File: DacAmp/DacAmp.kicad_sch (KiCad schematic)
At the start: 0 parts

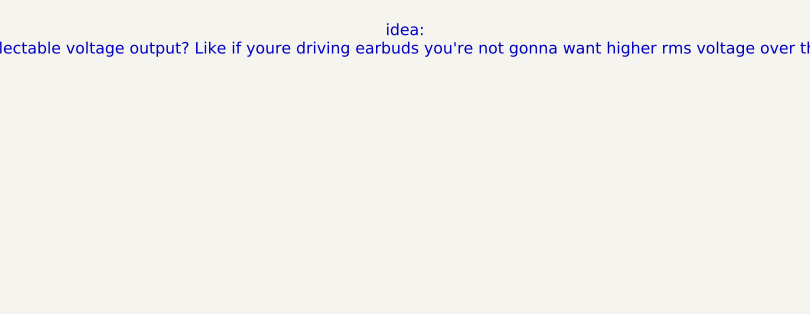
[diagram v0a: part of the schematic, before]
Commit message: add usb + codec
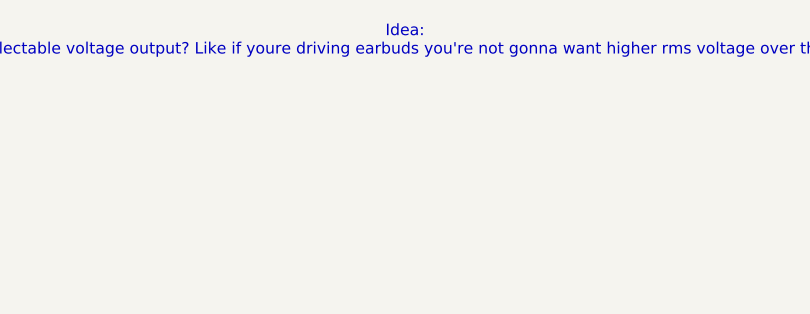
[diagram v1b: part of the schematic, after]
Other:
- note added: "Idea: Make selectable voltage output? Like if youre driving earbuds you're not gonna want higher rms voltage over the thing."
- note removed: "idea: Make selectable voltage output? Like if youre driving earbuds you're not gonna want higher rms voltage over the thing."
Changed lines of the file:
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@@
 	(generator_version "8.0")
 	(paper "A4")
-	(text "idea: \nMake selectable voltage output? Like if youre driving earbuds you're not gonna want higher rms voltage over the thing."
+	(text "Idea: \nMake selectable voltage output? Like if youre driving earbuds you're not gonna want higher rms voltage over the thing."
 		(exclude_from_sim no)
 		(at 217.424 24.13 0)

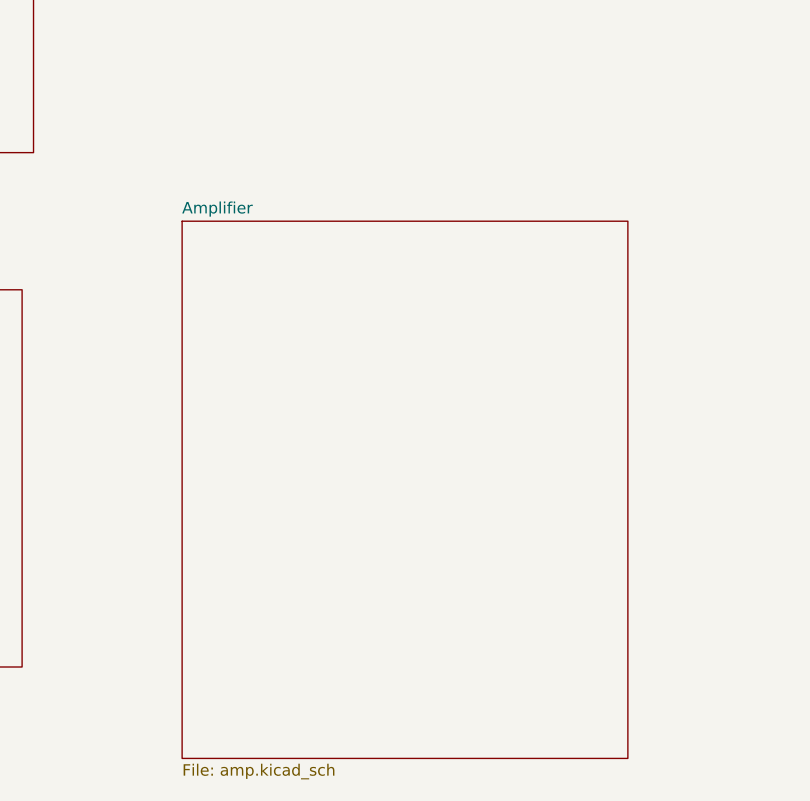
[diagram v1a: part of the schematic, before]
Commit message: add basic analog parts
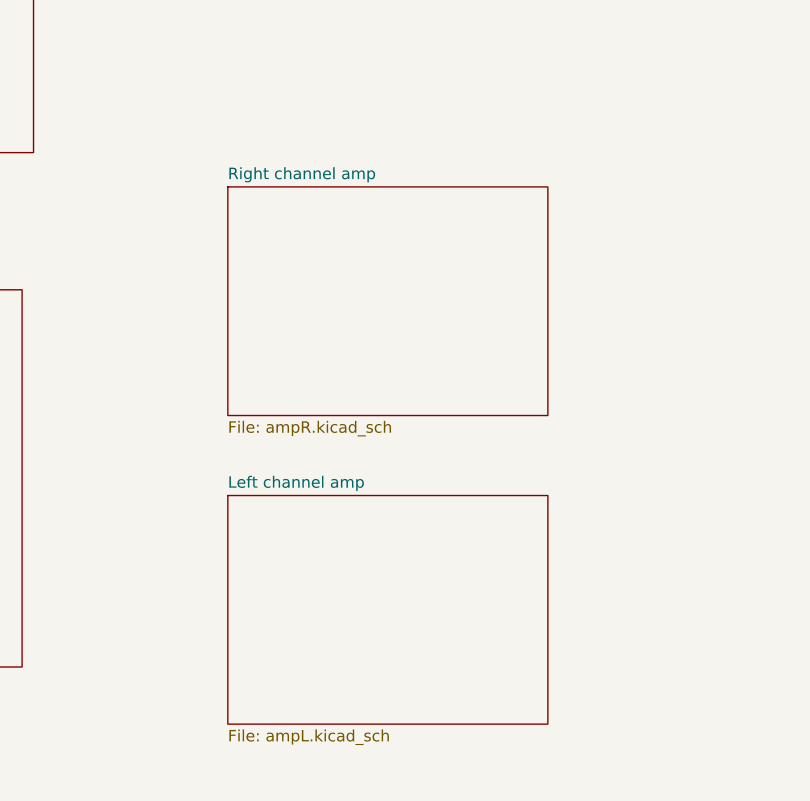
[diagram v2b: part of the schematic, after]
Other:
- removed sheet Amplifier
- added sheet Left channel amp (ampL.kicad_sch)
- added sheet Right channel amp (ampR.kicad_sch)
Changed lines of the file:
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@@
-	)
-	(sheet
-		(at 172.72 74.93)
-		(size 49.53 59.69)
-		(fields_autoplaced yes)
-		(stroke
-			(width 0.1524)
-			(type solid)
-		)
-		(fill
-			(color 0 0 0 0.0000)
-		)
-		(property "Sheetname" "Amplifier"
-			(at 172.72 74.2184 0)
-			(effects
-				(font
-					(size 1.27 1.27)
-				)
-				(justify left bottom)
-			)
-		)
-		(property "Sheetfile" "amp.kicad_sch"
-			(at 172.72 135.2046 0)
-			(effects
-				(font
-					(size 1.27 1.27)
-				)
-				(justify left top)
-			)
-		)
-		(instances
-			(project "DacAmp"
-				(path "/d6da33f4-6bef-4098-a08b-0ea38da216b8"
-					(page "4")
-				)
-			)
-		)
 	)
 	(sheet
@@
 				(path "/d6da33f4-6bef-4098-a08b-0ea38da216b8"
 					(page "2")
+				)
+			)
+		)
+	)
+	(sheet
+		(at 177.8 71.12)
+		(size 35.56 25.4)
+		(fields_autoplaced yes)
+		(stroke
+			(width 0.1524)
+			(type solid)
+		)
+		(fill
+			(color 0 0 0 0.0000)
+		)
+		(property "Sheetname" "Right channel amp"
+			(at 177.8 70.4084 0)
+			(effects
+				(font
+					(size 1.27 1.27)
+				)
+				(justify left bottom)
+			)
+		)
+		(property "Sheetfile" "ampR.kicad_sch"
+			(at 177.8 97.1046 0)
+			(effects
+				(font
+					(size 1.27 1.27)
+				)
+				(justify left top)
+			)
+		)
+		(instances
+			(project "DacAmp"
+				(path "/d6da33f4-6bef-4098-a08b-0ea38da216b8"
+					(page "5")
 				)
 			)
@@
 				)
 			)
+		)
+	)
+	(sheet
+		(at 177.8 105.41)
+		(size 35.56 25.4)
+		(fields_autoplaced yes)
+		(stroke
+			(width 0.1524)
+			(type solid)
+		)
+		(fill
+			(color 0 0 0 0.0000)
+		)
+		(property "Sheetname" "Left channel amp"
+			(at 177.8 104.6984 0)
+			(effects
+				(font
+					(size 1.27 1.27)
+				)
+				(justify left bottom)
+			)
+		)
+		(property "Sheetfile" "ampL.kicad_sch"
+			(at 177.8 131.3946 0)
+			(effects
+				(font
+					(size 1.27 1.27)
+				)
+				(justify left top)
+			)
+		)
+		(instances
+			(project "DacAmp"
+				(path "/d6da33f4-6bef-4098-a08b-0ea38da216b8"
+					(page "6")
+				)
+			)

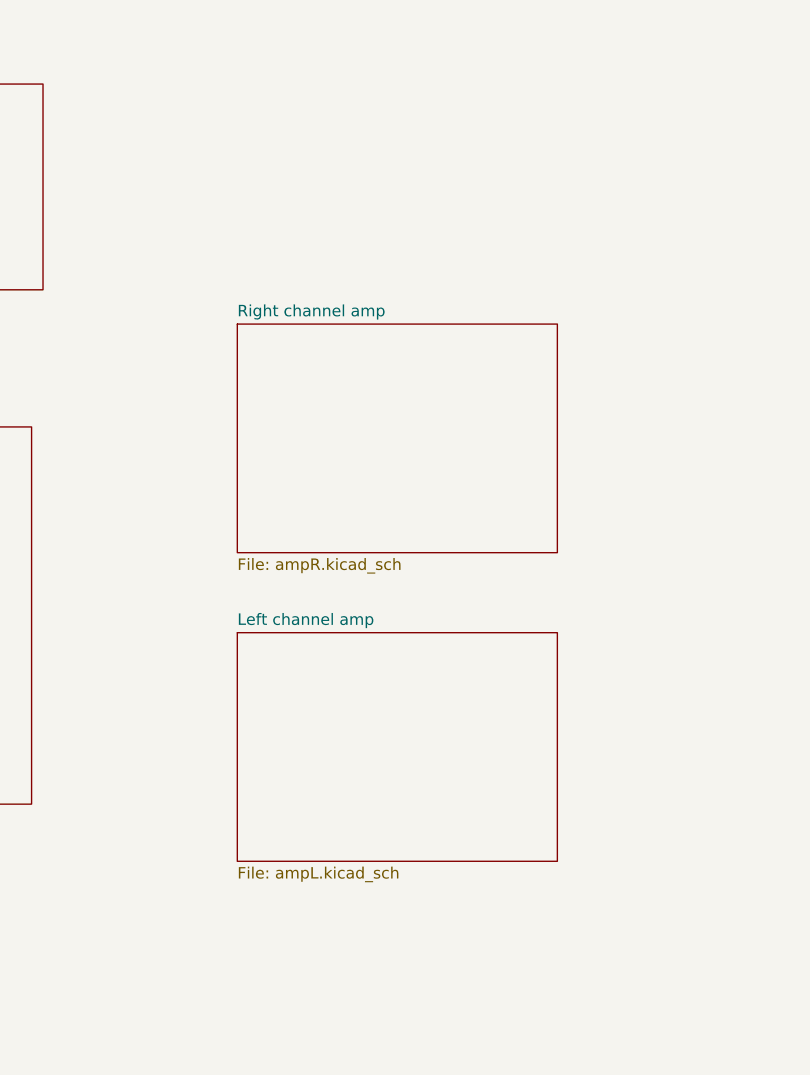
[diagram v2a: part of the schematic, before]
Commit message: add op amps to ampR
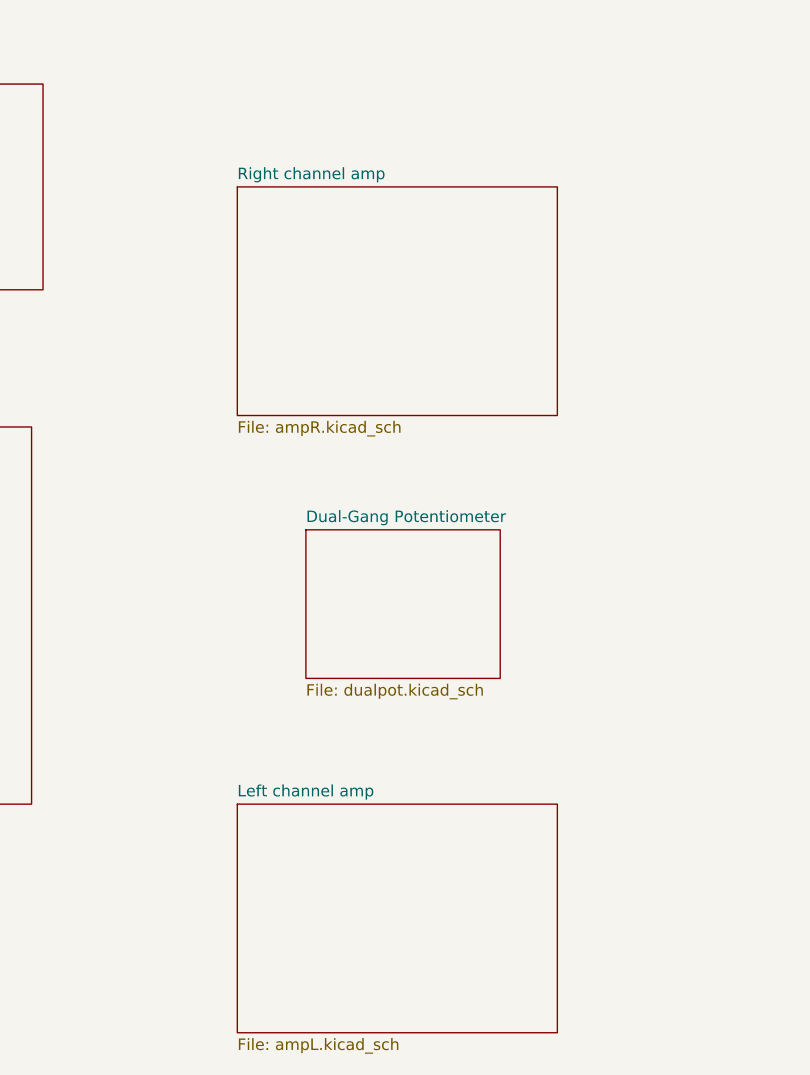
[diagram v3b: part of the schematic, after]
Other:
- added sheet Dual-Gang Potentiometer (dualpot.kicad_sch)
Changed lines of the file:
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@@
 	)
 	(sheet
-		(at 177.8 71.12)
+		(at 177.8 55.88)
 		(size 35.56 25.4)
 		(fields_autoplaced yes)
@@
 		)
 		(property "Sheetname" "Right channel amp"
-			(at 177.8 70.4084 0)
+			(at 177.8 55.1684 0)
 			(effects
 				(font
@@
 		)
 		(property "Sheetfile" "ampR.kicad_sch"
-			(at 177.8 97.1046 0)
+			(at 177.8 81.8646 0)
 			(effects
 				(font
@@
 				(path "/d6da33f4-6bef-4098-a08b-0ea38da216b8"
 					(page "5")
+				)
+			)
+		)
+	)
+	(sheet
+		(at 185.42 93.98)
+		(size 21.59 16.51)
+		(fields_autoplaced yes)
+		(stroke
+			(width 0.1524)
+			(type solid)
+		)
+		(fill
+			(color 0 0 0 0.0000)
+		)
+		(property "Sheetname" "Dual-Gang Potentiometer"
+			(at 185.42 93.2684 0)
+			(effects
+				(font
+					(size 1.27 1.27)
+				)
+				(justify left bottom)
+			)
+		)
+		(property "Sheetfile" "dualpot.kicad_sch"
+			(at 185.42 111.0746 0)
+			(effects
+				(font
+					(size 1.27 1.27)
+				)
+				(justify left top)
+			)
+		)
+		(instances
+			(project "DacAmp"
+				(path "/d6da33f4-6bef-4098-a08b-0ea38da216b8"
+					(page "7")
 				)
 			)
@@
 	)
 	(sheet
-		(at 177.8 105.41)
+		(at 177.8 124.46)
 		(size 35.56 25.4)
 		(fields_autoplaced yes)
@@
 		)
 		(property "Sheetname" "Left channel amp"
-			(at 177.8 104.6984 0)
+			(at 177.8 123.7484 0)
 			(effects
 				(font
@@
 		)
 		(property "Sheetfile" "ampL.kicad_sch"
-			(at 177.8 131.3946 0)
+			(at 177.8 150.4446 0)
 			(effects
 				(font

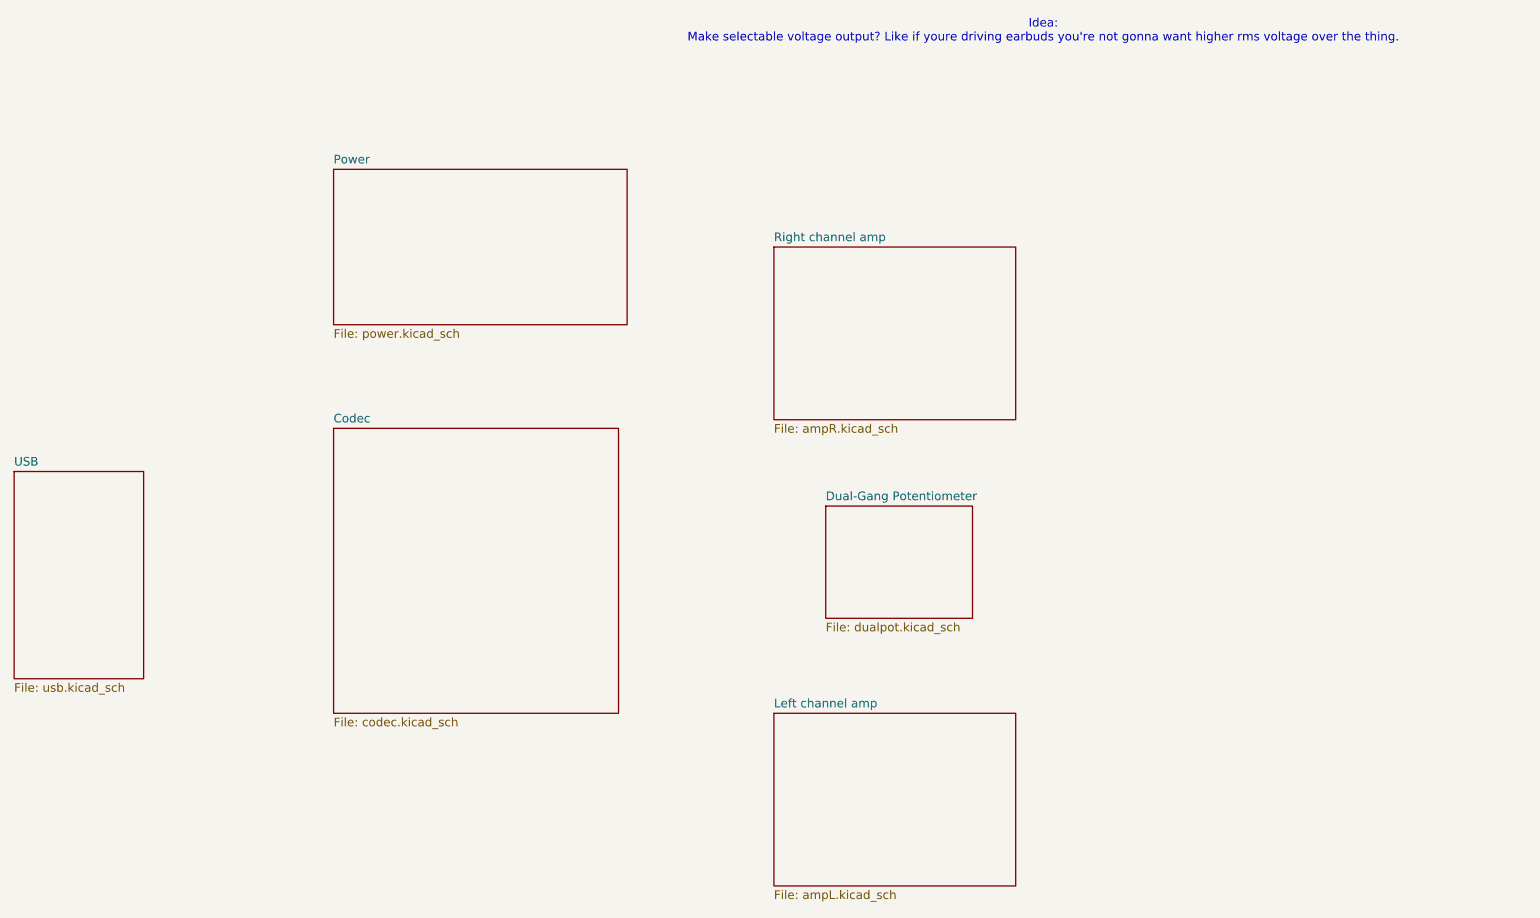
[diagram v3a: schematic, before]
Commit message: change sheet architecture
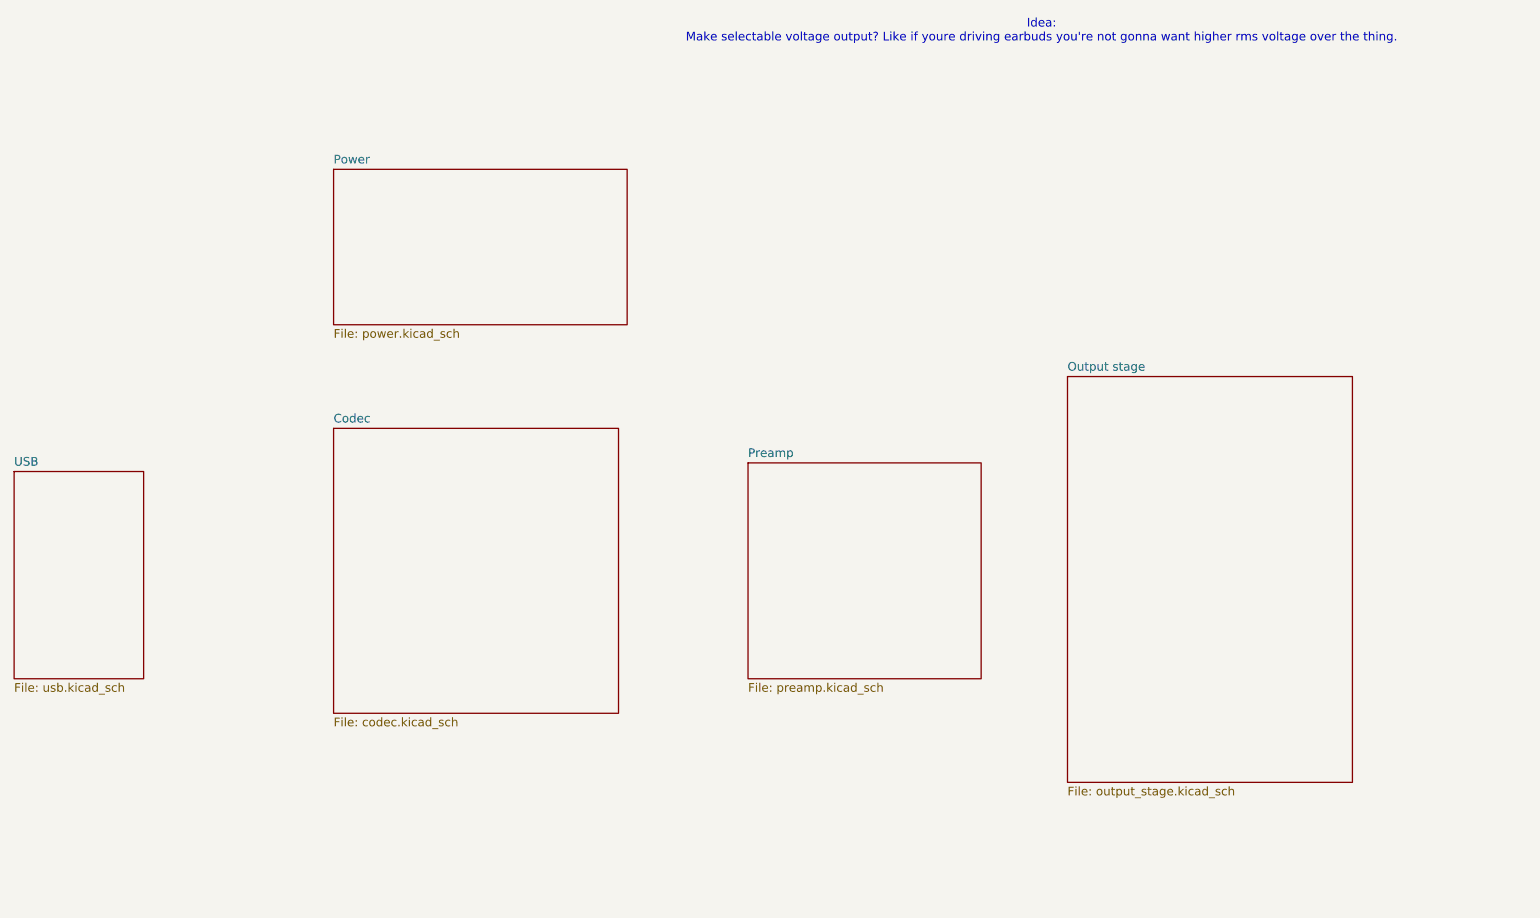
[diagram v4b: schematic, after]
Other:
- sheet Right channel amp renamed Preamp
- removed sheet Dual-Gang Potentiometer
- removed sheet Left channel amp
- added sheet Output stage (output_stage.kicad_sch)
- sheet Preamp: file ampR.kicad_sch -> preamp.kicad_sch
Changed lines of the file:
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@@
 	(text "Idea: \nMake selectable voltage output? Like if youre driving earbuds you're not gonna want higher rms voltage over the thing."
 		(exclude_from_sim no)
-		(at 217.424 24.13 0)
+		(at 217.17 24.13 0)
 		(effects
 			(font
 				(size 1.27 1.27)
+			)
+		)
+	)
+	(sheet
+		(at 220.98 74.93)
+		(size 41.91 59.69)
+		(fields_autoplaced yes)
+		(stroke
+			(width 0.1524)
+			(type solid)
+		)
+		(fill
+			(color 0 0 0 0.0000)
+		)
+		(property "Sheetname" "Output stage"
+			(at 220.98 74.2184 0)
+			(effects
+				(font
+					(size 1.27 1.27)
+				)
+				(justify left bottom)
+			)
+		)
+		(property "Sheetfile" "output_stage.kicad_sch"
+			(at 220.98 135.2046 0)
+			(effects
+				(font
+					(size 1.27 1.27)
+				)
+				(justify left top)
+			)
+		)
+		(instances
+			(project "DacAmp"
+				(path "/d6da33f4-6bef-4098-a08b-0ea38da216b8"
+					(page "7")
+				)
 			)
 		)
@@
 	)
 	(sheet
-		(at 177.8 55.88)
-		(size 35.56 25.4)
+		(at 173.99 87.63)
+		(size 34.29 31.75)
 		(fields_autoplaced yes)
 		(stroke
@@
 			(color 0 0 0 0.0000)
 		)
-		(property "Sheetname" "Right channel amp"
-			(at 177.8 55.1684 0)
+		(property "Sheetname" "Preamp"
+			(at 173.99 86.9184 0)
 			(effects
 				(font
@@
 			)
 		)
-		(property "Sheetfile" "ampR.kicad_sch"
-			(at 177.8 81.8646 0)
+		(property "Sheetfile" "preamp.kicad_sch"
+			(at 173.99 119.9646 0)
 			(effects
 				(font
@@
 				(path "/d6da33f4-6bef-4098-a08b-0ea38da216b8"
 					(page "5")
-				)
-			)
-		)
-	)
-	(sheet
-		(at 185.42 93.98)
-		(size 21.59 16.51)
-		(fields_autoplaced yes)
-		(stroke
-			(width 0.1524)
-			(type solid)
-		)
-		(fill
-			(color 0 0 0 0.0000)
-		)
-		(property "Sheetname" "Dual-Gang Potentiometer"
-			(at 185.42 93.2684 0)
-			(effects
-				(font
-					(size 1.27 1.27)
-				)
-				(justify left bottom)
-			)
-		)
-		(property "Sheetfile" "dualpot.kicad_sch"
-			(at 185.42 111.0746 0)
-			(effects
-				(font
-					(size 1.27 1.27)
-				)
-				(justify left top)
-			)
-		)
-		(instances
-			(project "DacAmp"
-				(path "/d6da33f4-6bef-4098-a08b-0ea38da216b8"
-					(page "7")
 				)
 			)
@@
 				)
 			)
-		)
-	)
-	(sheet
-		(at 177.8 124.46)
-		(size 35.56 25.4)
-		(fields_autoplaced yes)
-		(stroke
-			(width 0.1524)
-			(type solid)
-		)
-		(fill
-			(color 0 0 0 0.0000)
-		)
-		(property "Sheetname" "Left channel amp"
-			(at 177.8 123.7484 0)
-			(effects
-				(font
-					(size 1.27 1.27)
-				)
-				(justify left bottom)
-			)
-		)
-		(property "Sheetfile" "ampL.kicad_sch"
-			(at 177.8 150.4446 0)
-			(effects
-				(font
-					(size 1.27 1.27)
-				)
-				(justify left top)
-			)
-		)
-		(instances
-			(project "DacAmp"
-				(path "/d6da33f4-6bef-4098-a08b-0ea38da216b8"
-					(page "6")
-				)
-			)
